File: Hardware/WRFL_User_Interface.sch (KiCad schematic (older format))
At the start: 11 parts, among them P15 1x8_2_54_FEM, Q3 SI1012CR, SW1 TSA12110, SW2 EN11-HSB, SW3 TSA12110, U9 S25FL216K0PMFI040

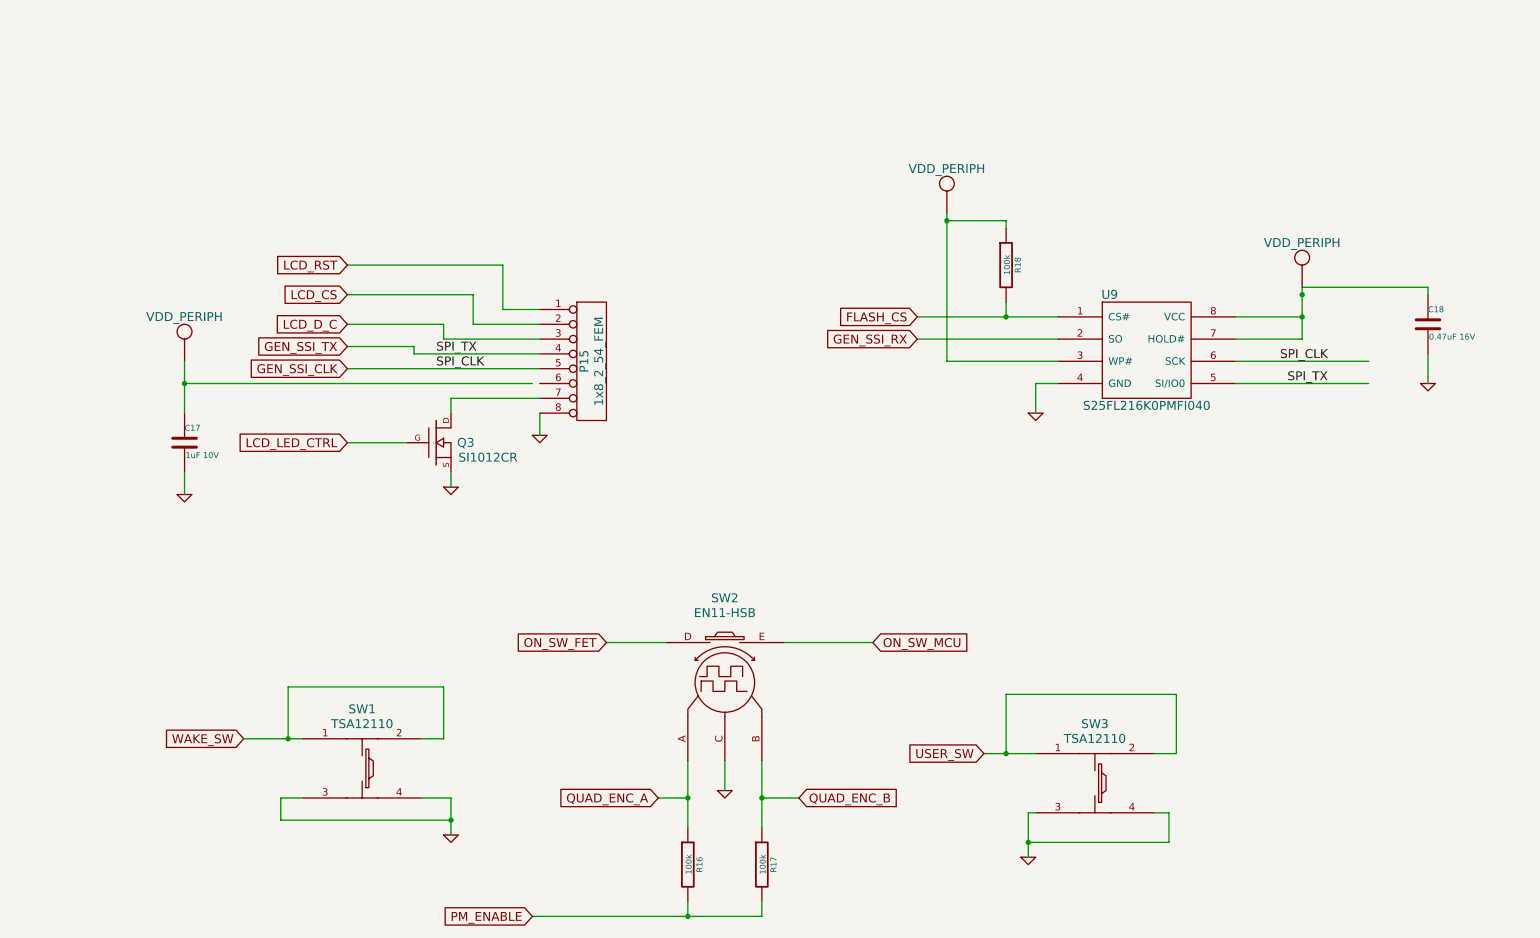
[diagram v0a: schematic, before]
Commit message: Added VREF and 2x3 for servos
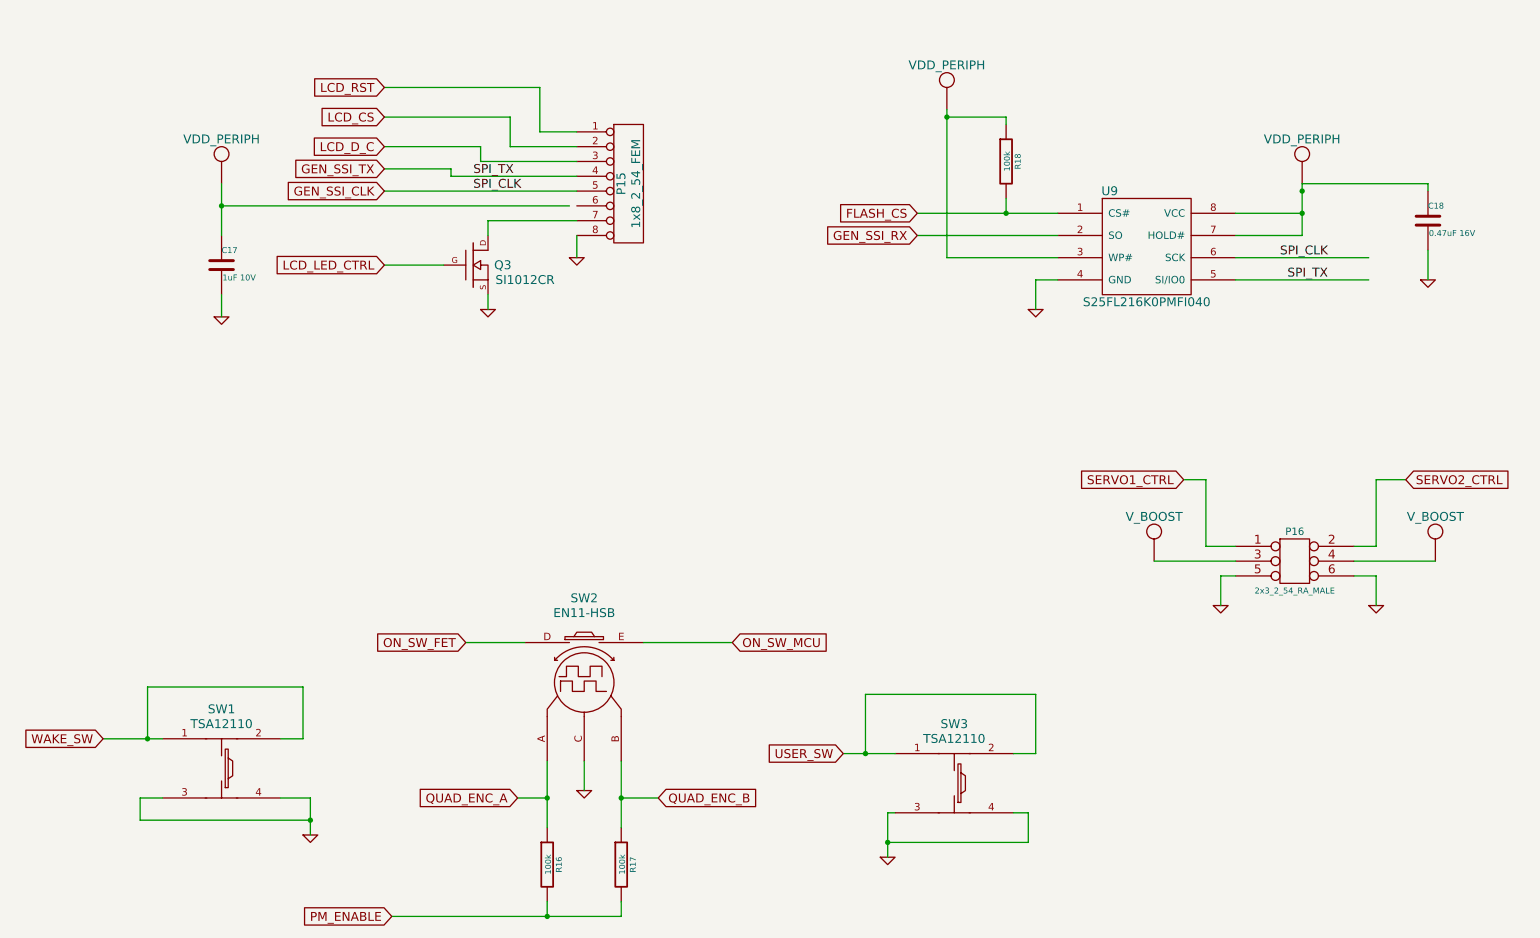
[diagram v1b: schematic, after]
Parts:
- added P16: 2x3_2_54_RA_MALE, symbol CONN_3X2
- added U7, U8: V_BOOST, ~, symbol V_BOOST
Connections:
- net labels added: SERVO1_CTRL, SERVO2_CTRL
- wire segments 68 -> 80
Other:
- moved on the sheet: C17, C18, P15, Q3, R16, R17, R18, SW1, SW2, SW3, U9

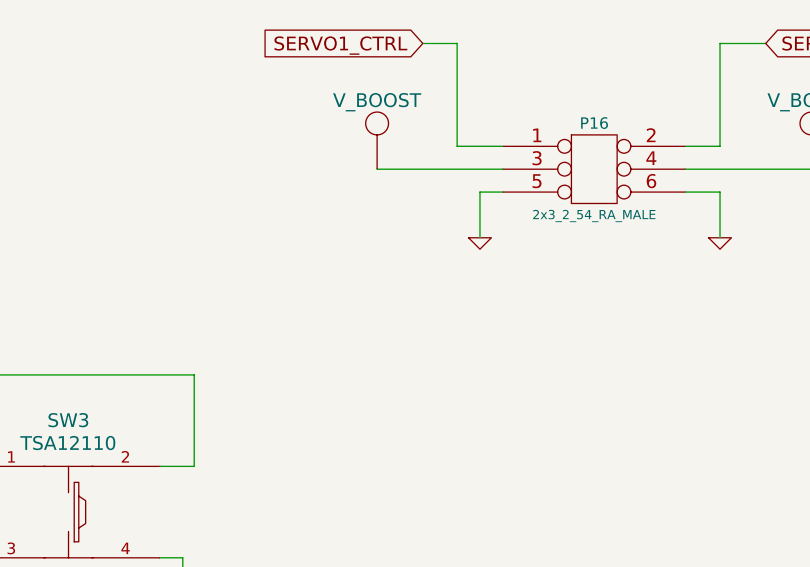
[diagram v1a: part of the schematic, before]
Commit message: Added VBAT sens
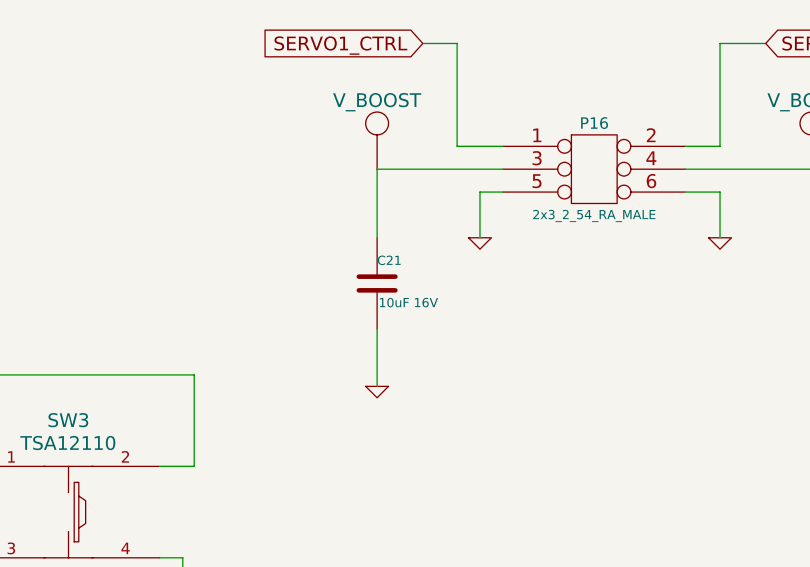
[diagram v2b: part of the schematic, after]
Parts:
- removed U7, U8: V_BOOST, ~, symbol V_BOOST
- added C21: 10uF 16V, 0805, symbol C
- SW2: footprint (none) -> EN11-HSB
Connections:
- net labels added: V_BOOST
- wire segments 80 -> 82
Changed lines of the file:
@@
-EESchema Schematic File Version 2  date 10/7/2013 7:37:21 AM
+EESchema Schematic File Version 2  date Monday, October 07, 2013 09:14:17 AM
 LIBS:power
 LIBS:device
@@
 F 0 "SW2" H 4450 5450 60  0000 C CNN
 F 1 "EN11-HSB" H 4450 5350 60  0000 C CNN
-F 2 "" H 4450 5030 60  0000 C CNN
+F 2 "EN11-HSB" H 4450 5030 60  0001 C CNN
 F 3 "" H 4450 5030 60  0000 C CNN
 	1    4450 5050
@@
 GEN_SSI_CLK
 $Comp
-L VDD_PERIPH #U11
+L VDD_PERIPH #U12
 U 1 1 5251E2C5
 P 2000 1650
-F 0 "#U11" H 2000 1850 60  0001 C CNN
+F 0 "#U12" H 2000 1850 60  0001 C CNN
 F 1 "VDD_PERIPH" H 2000 1750 60  0000 C CNN
 F 2 "~" H 2000 1650 60  0000 C CNN
@@
 $EndComp
 $Comp
-L VDD_PERIPH #U13
+L VDD_PERIPH #U14
 U 1 1 5251E301
 P 9300 1650
-F 0 "#U13" H 9300 1850 60  0001 C CNN
+F 0 "#U14" H 9300 1850 60  0001 C CNN
 F 1 "VDD_PERIPH" H 9300 1750 60  0000 C CNN
 F 2 "~" H 9300 1650 60  0000 C CNN
@@
 $EndComp
 $Comp
-L GND #PWR29
+L GND #PWR31
 U 1 1 5251E310
 P 2000 2750
-F 0 "#PWR29" H 2000 2750 30  0001 C CNN
+F 0 "#PWR31" H 2000 2750 30  0001 C CNN
 F 1 "GND" H 2000 2680 30  0001 C CNN
 F 2 "" H 2000 2750 60  0000 C CNN
@@
 $EndComp
 $Comp
-L GND #PWR30
+L GND #PWR32
 U 1 1 5251E31F
 P 2600 6250
-F 0 "#PWR30" H 2600 6250 30  0001 C CNN
+F 0 "#PWR32" H 2600 6250 30  0001 C CNN
 F 1 "GND" H 2600 6180 30  0001 C CNN
 F 2 "" H 2600 6250 60  0000 C CNN
@@
 $EndComp
 $Comp
-L GND #PWR33
+L GND #PWR35
 U 1 1 5251E32E
 P 4450 5950
-F 0 "#PWR33" H 4450 5950 30  0001 C CNN
+F 0 "#PWR35" H 4450 5950 30  0001 C CNN
 F 1 "GND" H 4450 5880 30  0001 C CNN
 F 2 "" H 4450 5950 60  0000 C CNN
@@
 $EndComp
 $Comp
-L GND #PWR34
+L GND #PWR36
 U 1 1 5251E33D
 P 6500 6400
-F 0 "#PWR34" H 6500 6400 30  0001 C CNN
+F 0 "#PWR36" H 6500 6400 30  0001 C CNN
 F 1 "GND" H 6500 6330 30  0001 C CNN
 F 2 "" H 6500 6400 60  0000 C CNN
@@
 $EndComp
 $Comp
-L GND #PWR32
+L GND #PWR34
 U 1 1 5251E34C
 P 4400 2350
-F 0 "#PWR32" H 4400 2350 30  0001 C CNN
+F 0 "#PWR34" H 4400 2350 30  0001 C CNN
 F 1 "GND" H 4400 2280 30  0001 C CNN
 F 2 "" H 4400 2350 60  0000 C CNN
@@
 $EndComp
 $Comp
-L GND #PWR35
+L GND #PWR37
 U 1 1 5251E35B
 P 7500 2700
-F 0 "#PWR35" H 7500 2700 30  0001 C CNN
+F 0 "#PWR37" H 7500 2700 30  0001 C CNN
 F 1 "GND" H 7500 2630 30  0001 C CNN
 F 2 "" H 7500 2700 60  0000 C CNN
@@
 	4400 2200 4400 2350
 $Comp
-L GND #PWR31
+L GND #PWR33
 U 1 1 5251E3CC
 P 3800 2700
-F 0 "#PWR31" H 3800 2700 30  0001 C CNN
+F 0 "#PWR33" H 3800 2700 30  0001 C CNN
 F 1 "GND" H 3800 2630 30  0001 C CNN
 F 2 "" H 3800 2700 60  0000 C CNN
@@
 $EndComp
 $Comp
-L GND #PWR38
+L GND #PWR41
 U 1 1 5251EA53
 P 10150 2500
-F 0 "#PWR38" H 10150 2500 30  0001 C CNN
+F 0 "#PWR41" H 10150 2500 30  0001 C CNN
 F 1 "GND" H 10150 2430 30  0001 C CNN
 F 2 "" H 10150 2500 60  0000 C CNN
@@
 	10150 1850 10150 1900
 $Comp
-L VDD_PERIPH #U12
+L VDD_PERIPH #U13
 U 1 1 5251EAB9
 P 6900 1150
-F 0 "#U12" H 6900 1350 60  0001 C CNN
+F 0 "#U13" H 6900 1350 60  0001 C CNN
 F 1 "VDD_PERIPH" H 6900 1250 60  0000 C CNN
 F 2 "~" H 6900 1150 60  0000 C CNN
@@
 $EndComp
 $Comp
-L GND #PWR37
+L GND #PWR40
 U 1 1 52523A67
 P 9800 4700
-F 0 "#PWR37" H 9800 4700 30  0001 C CNN
+F 0 "#PWR40" H 9800 4700 30  0001 C CNN
 F 1 "GND" H 9800 4630 30  0001 C CNN
 F 2 "" H 9800 4700 60  0000 C CNN
@@
 $EndComp
 $Comp
-L GND #PWR36
+L GND #PWR39
 U 1 1 52523A76
 P 8750 4700
-F 0 "#PWR36" H 8750 4700 30  0001 C CNN
+F 0 "#PWR39" H 8750 4700 30  0001 C CNN
 F 1 "GND" H 8750 4630 30  0001 C CNN
 F 2 "" H 8750 4700 60  0000 C CNN
@@
 	9800 4500 9800 4700
 $Comp
-L V_BOOST U7
+L V_BOOST #U7
 U 1 1 52523B29
 P 8300 4200
-F 0 "U7" H 8300 4400 60  0001 C CNN
+F 0 "#U7" H 8300 4400 60  0001 C CNN
 F 1 "V_BOOST" H 8300 4300 60  0000 C CNN
 F 2 "~" H 8300 4200 60  0000 C CNN
@@
 $EndComp
 $Comp
-L V_BOOST U8
+L V_BOOST #U8
 U 1 1 52523B38
 P 10200 4200
-F 0 "U8" H 10200 4400 60  0001 C CNN
+F 0 "#U8" H 10200 4400 60  0001 C CNN
 F 1 "V_BOOST" H 10200 4300 60  0000 C CNN
 F 2 "~" H 10200 4200 60  0000 C CNN
@@
 Wire Wire Line
 	8650 4300 8850 4300
+$Comp
+L C C21
+U 1 1 52526585
+P 8300 4900
+F 0 "C21" H 8300 5000 40  0000 L CNN
+F 1 "10uF 16V" H 8306 4815 40  0000 L CNN
+F 2 "0805" H 8338 4750 30  0001 C CNN
+F 3 "~" H 8300 4900 60  0000 C CNN
+	1    8300 4900
+	1    0    0    -1
+$EndComp
+$Comp
+L GND #PWR38
+U 1 1 52526592
+P 8300 5350
+F 0 "#PWR38" H 8300 5350 30  0001 C CNN
+F 1 "GND" H 8300 5280 30  0001 C CNN
+F 2 "" H 8300 5350 60  0000 C CNN
+F 3 "" H 8300 5350 60  0000 C CNN
+	1    8300 5350
+	1    0    0    -1
+$EndComp
+Wire Wire Line
+	8300 4700 8300 4400
+Wire Wire Line
+	8300 5100 8300 5350
 $EndSCHEMATC

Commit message: added footprint values for caps and resistors
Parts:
- C17, C18, R16, R17, R18: footprint ~ -> 0805
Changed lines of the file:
@@
-EESchema Schematic File Version 2  date Monday, October 07, 2013 09:14:17 AM
+EESchema Schematic File Version 2  date Monday, October 07, 2013 12:52:48 PM
 LIBS:power
 LIBS:device
@@
 F 0 "C17" H 2000 2500 40  0000 L CNN
 F 1 "1uF 10V" H 2006 2315 40  0000 L CNN
-F 2 "~" H 2038 2250 30  0000 C CNN
+F 2 "0805" H 2038 2250 30  0001 C CNN
 F 3 "~" H 2000 2400 60  0000 C CNN
 	1    2000 2400
@@
 F 0 "C18" H 10150 2200 40  0000 L CNN
 F 1 "0.47uF 16V" H 10156 2015 40  0000 L CNN
-F 2 "~" H 10188 1950 30  0000 C CNN
+F 2 "0805" H 10188 1950 30  0001 C CNN
 F 3 "~" H 10150 2100 60  0000 C CNN
 	1    10150 2100
@@
 F 0 "R18" V 7380 1700 40  0000 C CNN
 F 1 "100k" V 7307 1701 40  0000 C CNN
-F 2 "~" V 7230 1700 30  0000 C CNN
+F 2 "0805" V 7230 1700 30  0001 C CNN
 F 3 "~" H 7300 1700 30  0000 C CNN
 	1    7300 1700
@@
 F 0 "R16" V 4280 6450 40  0000 C CNN
 F 1 "100k" V 4207 6451 40  0000 C CNN
-F 2 "~" V 4130 6450 30  0000 C CNN
+F 2 "0805" V 4130 6450 30  0001 C CNN
 F 3 "~" H 4200 6450 30  0000 C CNN
 	1    4200 6450
@@
 F 0 "R17" V 4780 6450 40  0000 C CNN
 F 1 "100k" V 4707 6451 40  0000 C CNN
-F 2 "~" V 4630 6450 30  0000 C CNN
+F 2 "0805" V 4630 6450 30  0001 C CNN
 F 3 "~" H 4700 6450 30  0000 C CNN
 	1    4700 6450
